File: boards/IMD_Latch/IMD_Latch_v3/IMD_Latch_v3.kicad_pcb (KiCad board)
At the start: 2 copper layers, 37 x 32 mm, 17 parts, among them J1 micromatch_female_RA_8, J2 Ultrafit_2, K1 G5Q-1A4-DC5-5V, Q1 SSM3K333R, U1 CD4043BPWR

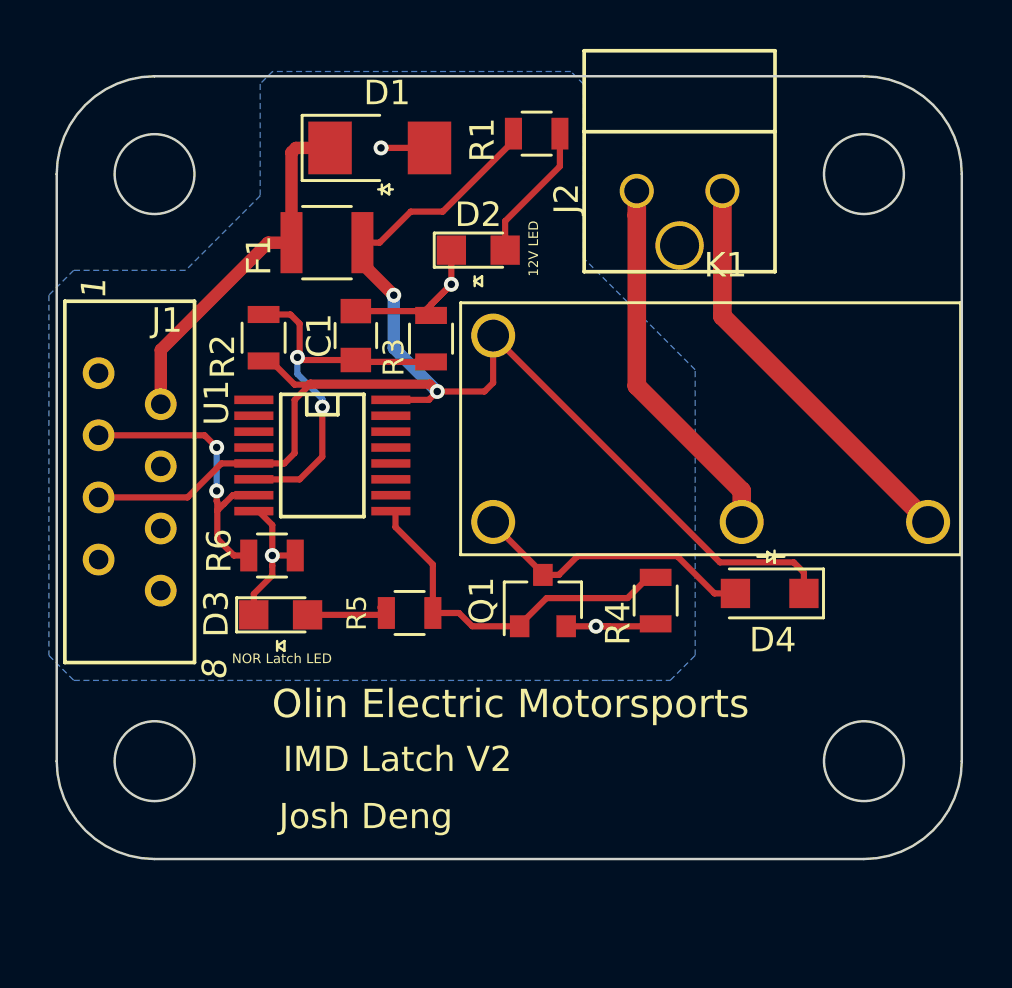
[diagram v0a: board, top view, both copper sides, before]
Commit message: Restored original air folder
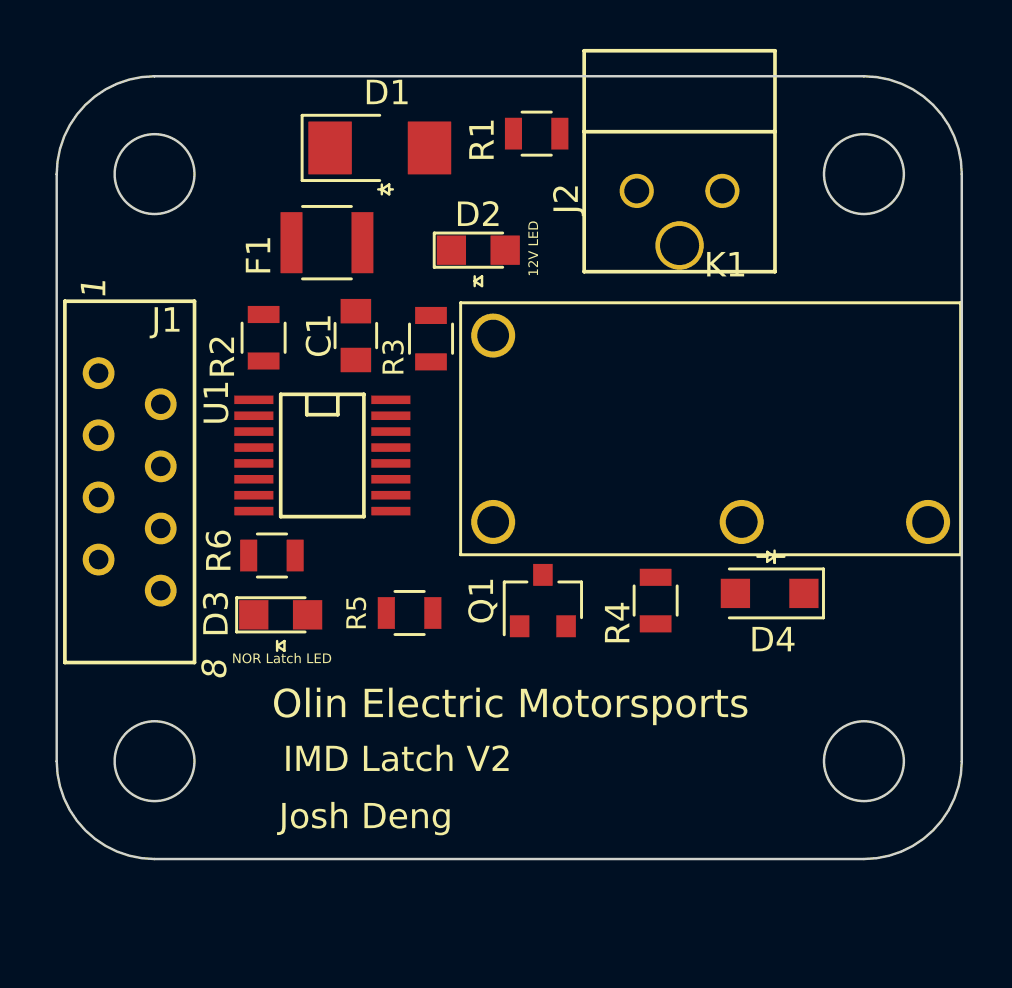
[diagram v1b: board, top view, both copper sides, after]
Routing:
- net /12V_Fused: track 59.8 -> 0.00 mm, vias 2 -> 0
- net GND: track 19.5 -> 0.00 mm, vias 4 -> 0
- net Net-(J2-Pad2): track 17.0 -> 0.00 mm
- net Net-(C1-Pad1): track 16.1 -> 0.00 mm, vias 2 -> 0
- net Net-(J2-Pad1): track 15.3 -> 0.00 mm
- net Net-(Q1-Pad1): track 15.0 -> 0.00 mm
- net +12V: track 14.7 -> 0.00 mm
- net Net-(J1-Pad3): track 12.3 -> 0.00 mm, vias 2 -> 0
- net Net-(D4-Pad2): track 11.9 -> 0.00 mm
- net Net-(D2-Pad2): track 5.69 -> 0.00 mm
- net Net-(D3-Pad2): track 3.27 -> 0.00 mm
- removed copper zone on B.Cu, net GND

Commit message: IMD v3 with layout
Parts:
- added G***: LOGO, footprints:Logo_Large, B.Cu at (159.0, 107.2)
- added G***: LOGO, footprints:Olin_O, B.Cu at (156.2, 95.8)
- added Q2: SSM3K333R, footprints:SOT-23F, F.Cu at (158.3, 102.2)
- added R7: R_604k, footprints:R_0805_OEM, F.Cu at (152.4, 114.2)
- added R8: R_604k, footprints:R_0805_OEM, F.Cu at (150.2, 95.4)
- added U2: TLV3701QDBVRG4Q1, footprints:SOT-23-5_OEM, F.Cu at (154.1, 102.5)
- C1: value C_10uF -> C_10uF_16V
- R2: value R_576k -> R_200k
- R3: value R_2.94M -> R_604k
- R4: value R_1M -> R_120k
- moved R5 19.8 mm to (158.9, 93.6), turned to 270 degrees
- moved R6 17.8 mm to (150.2, 92.8), turned to 180 degrees
- moved D3 17.4 mm to (158.5, 98.1), turned to 90 degrees
- moved R1 17.4 mm to (150.9, 108.3), turned to 270 degrees
- moved D2 17.0 mm to (148.3, 112.4)
- moved D4 15.1 mm to (154.3, 110.5), turned to 270 degrees
- moved C1 14.9 mm to (152.5, 116.5), turned to 180 degrees
- moved R4 12.3 mm to (153.8, 106.6), turned to 180 degrees
- moved U1 11.2 mm to (154.5, 95.9), turned to 0 degrees
- moved Q1 10.8 mm to (163.4, 102.1), turned to 0 degrees
- moved F1 10.8 mm to (147.8, 108.0), turned to 270 degrees
- moved D1 9.03 mm to (148.0, 101.1), turned to 90 degrees
- moved R3 5.39 mm to (150.8, 99.1)
- moved K1 4.16 mm to (157.4, 113.3)
- moved R2 2.88 mm to (150.8, 103.6), turned to 90 degrees
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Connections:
- D3 pad 1: GND -> Net-(D3-Pad1)
- J1 pad 8: Net-(J1-Pad8) -> /IMD_Status_Output
- Q1 pad 1: Net-(Q1-Pad1) -> /IMD_Status_Output
- R2 pad 1: Net-(C1-Pad1) -> /12V_Fused
- R2 pad 2: /12V_Fused -> Net-(R2-Pad2)
- R3 pad 1: Net-(C1-Pad1) -> Net-(R2-Pad2)
- R4 pad 1: Net-(Q1-Pad1) -> Net-(C1-Pad1)
- R4 pad 2: GND -> /12V_Fused
- R5 pad 1: Net-(Q1-Pad1) -> /12V_Fused
- U1 pad 1: Net-(U1-Pad1) -> (no net)
- U1 pad 10: Net-(U1-Pad10) -> (no net)
- U1 pad 11: Net-(U1-Pad11) -> (no net)
- U1 pad 12: Net-(U1-Pad12) -> (no net)
- U1 pad 13: Net-(U1-Pad13) -> (no net)
- U1 pad 14: Net-(U1-Pad14) -> (no net)
- U1 pad 15: Net-(U1-Pad15) -> (no net)
- U1 pad 2: Net-(U1-Pad2) -> /IMD_Status_Output
- U1 pad 3: Net-(U1-Pad3) -> Net-(J1-Pad3)
- U1 pad 6: Net-(C1-Pad1) -> (no net)
- U1 pad 7: Net-(J1-Pad3) -> (no net)
- U1 pad 9: Net-(Q1-Pad1) -> (no net)
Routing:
- net /12V_Fused: track 0.00 -> 51.3 mm, vias 0 -> 3
- net /IMD_Status_Output: track 0.00 -> 35.7 mm, vias 0 -> 5
- net Net-(J1-Pad3): track 0.00 -> 30.9 mm
- net GND: track 0.00 -> 30.6 mm, vias 0 -> 5
- net Net-(J2-Pad2): track 0.00 -> 20.7 mm
- net Net-(J2-Pad1): track 0.00 -> 19.0 mm
- net Net-(D4-Pad2): track 0.00 -> 17.8 mm
- net Net-(C1-Pad1): track 0.00 -> 15.2 mm
- net Net-(D3-Pad1): track 0.00 -> 10.4 mm
- net +12V: track 0.00 -> 8.30 mm
- net Net-(R2-Pad2): track 0.00 -> 7.53 mm
- net Net-(D2-Pad2): track 0.00 -> 4.34 mm
- net Net-(U1-Pad4): track 0.00 -> 3.35 mm
- net Net-(D3-Pad2): track 0.00 -> 2.40 mm
- added copper zone on B.Cu, net GND
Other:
- board text added: "IMD Latch V3"
- board text added: "Latch LED"
- board text removed: "IMD Latch V2"
- board text removed: "NOR Latch LED"

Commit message: IMD Latch v3 for review
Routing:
- net Net-(J2-Pad2): track 20.7 -> 40.8 mm
- net Net-(J2-Pad1): track 19.0 -> 37.3 mm
- net GND: track 30.6 -> 35.2 mm
- net /12V_Fused: track 51.3 -> 54.2 mm
- net Net-(D3-Pad1): track 10.4 -> 11.0 mm
- net Net-(C1-Pad1): track 15.2 -> 14.6 mm
- net Net-(D2-Pad2): track 4.34 -> 3.84 mm

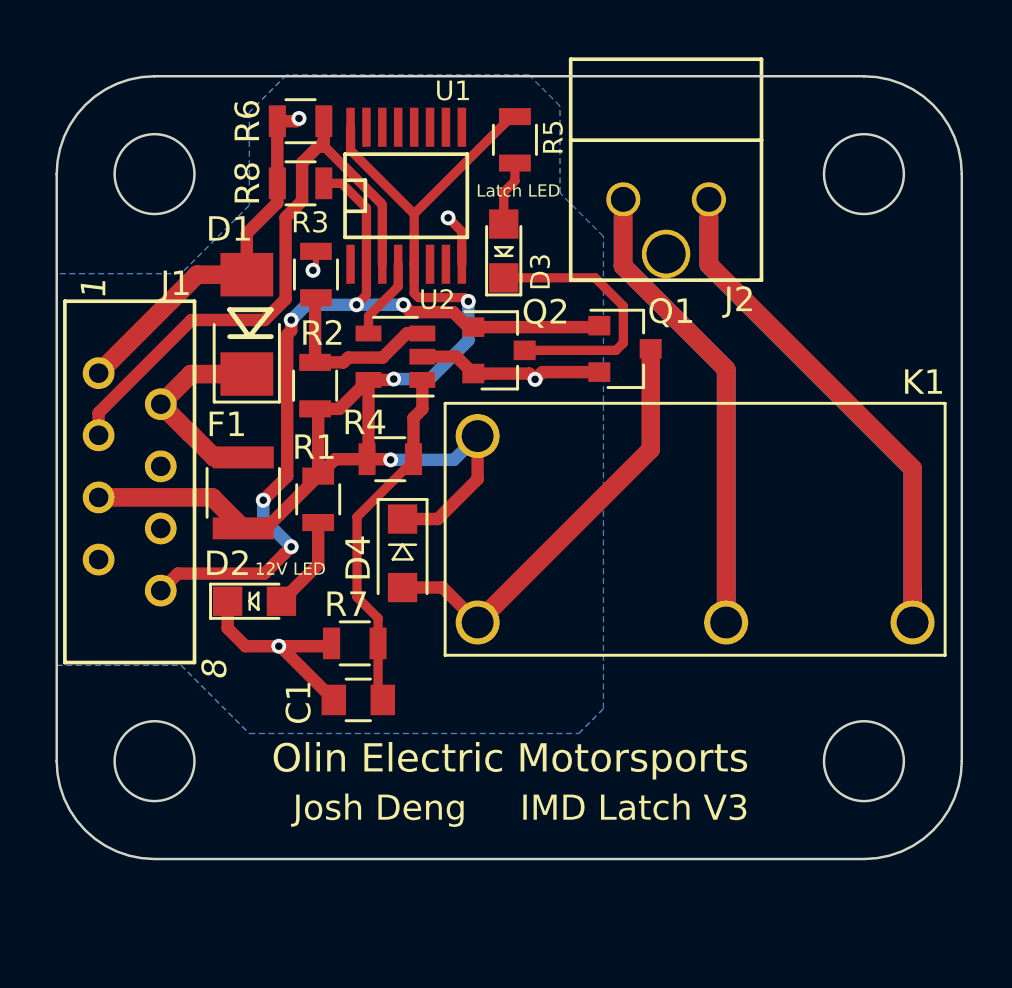
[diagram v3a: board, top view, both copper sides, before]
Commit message: IMD Latch connector redesigned
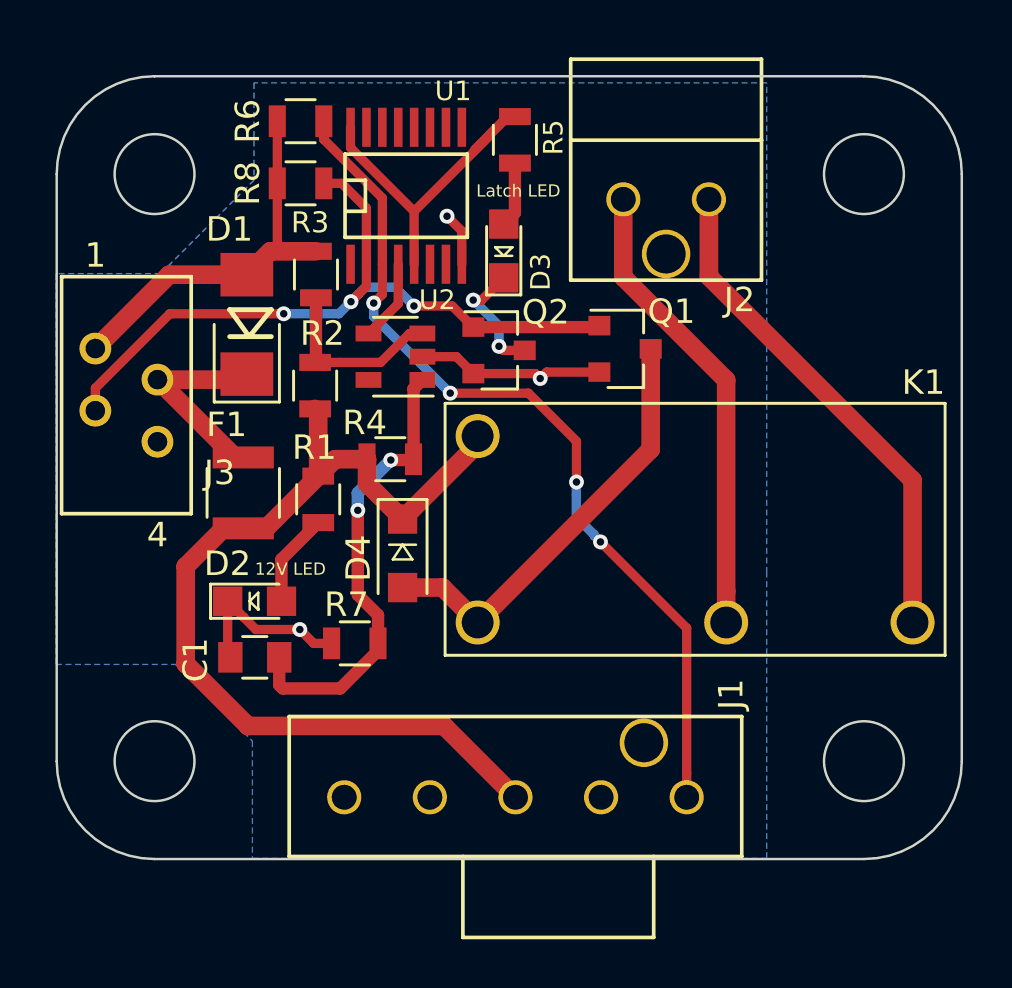
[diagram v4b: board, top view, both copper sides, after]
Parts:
- removed G***: LOGO, footprints:Logo_Large
- removed G***: LOGO, footprints:Olin_O
- added J3: micromatch_female_RA_4, footprints:micromatch_female_ra_4, F.Cu at (141.8, 107.2)
- J1: value micromatch_female_RA_8 -> Ultrafit_5; footprint footprints:micromatch_female_ra_8 -> footprints:Ultrafit_5
- moved J1 22.4 mm to (160.7, 120.5), turned to 90 degrees
- moved C1 4.57 mm to (148.3, 114.7)
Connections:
- J1 pad 1: GND -> Net-(J1-Pad1)
- J1 pad 2: +12V -> GND
- J1 pad 3: Net-(J1-Pad3) -> /12V_Fused
- J1 pad 5: /12V_Fused -> GND
- R6 pad 1: Net-(J1-Pad3) -> Net-(J1-Pad1)
- U1 pad 3: Net-(J1-Pad3) -> Net-(J1-Pad1)
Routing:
- net Net-(J1-Pad1): track 0.00 -> 36.0 mm, vias 0 -> 4
- net Net-(J1-Pad3): track 31.2 -> 0.00 mm
- net Net-(J2-Pad2): track 40.8 -> 20.7 mm
- net Net-(J2-Pad1): track 37.3 -> 19.0 mm
- net Net-(D3-Pad1): track 11.0 -> 5.07 mm, vias 0 -> 2
- net /IMD_Status_Output: track 35.9 -> 30.2 mm, vias 5 -> 3
- net Net-(C1-Pad1): track 14.6 -> 18.9 mm, vias 0 -> 2
- net GND: track 35.2 -> 34.8 mm, vias 5 -> 3
- net /12V_Fused: track 54.2 -> 53.8 mm, vias 3 -> 0
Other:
- board text removed: "Olin Electric Motorsports"

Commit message: IMD Latch v3 to ship
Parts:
- added C2: C_10uF_16V, footprints:C_0805_OEM, F.Cu at (143.0, 110.3)
- J3: value micromatch_female_RA_4 -> micromatch_female_TOP_ENTRY_locking_4; footprint footprints:micromatch_female_ra_4 -> footprints:micromatch_female_vert_4
- moved J3 0.18 mm to (141.9, 107.3)
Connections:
- J3 pad 4: (no net) -> GND
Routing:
- net /12V_Fused: track 53.8 -> 70.2 mm, vias 0 -> 1
- net GND: track 34.8 -> 41.7 mm
